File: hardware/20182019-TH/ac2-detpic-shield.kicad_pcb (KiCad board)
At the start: 2 copper layers, 99.1 x 69.6 mm, 57 parts, among them J1 HEADER, J2 HEADER, J3 HEADER, J4 HEADER, J5 HEADER, J6 HEADER, J7 HEADER, M1 M1, M2 M2, M3 MountingHole_2.2mm_M2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

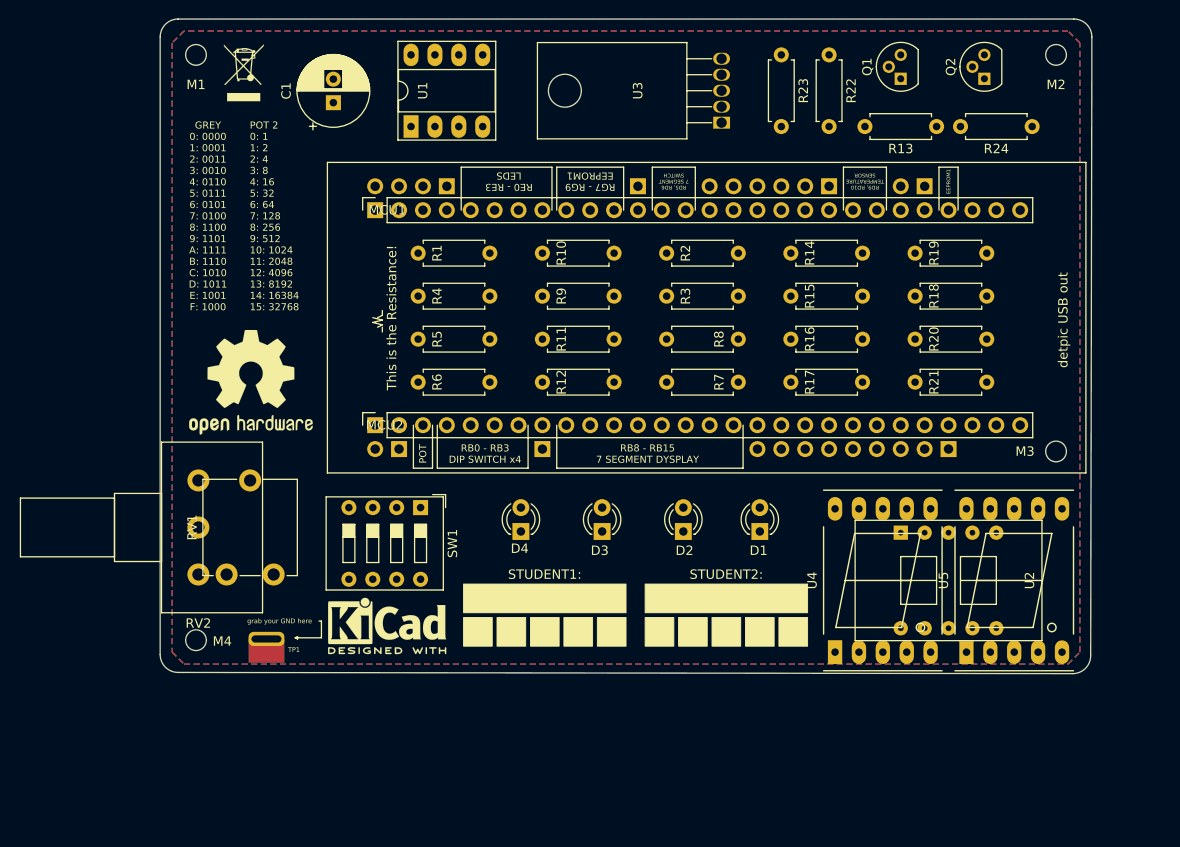
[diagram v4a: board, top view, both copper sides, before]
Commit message: small pcb organization of components
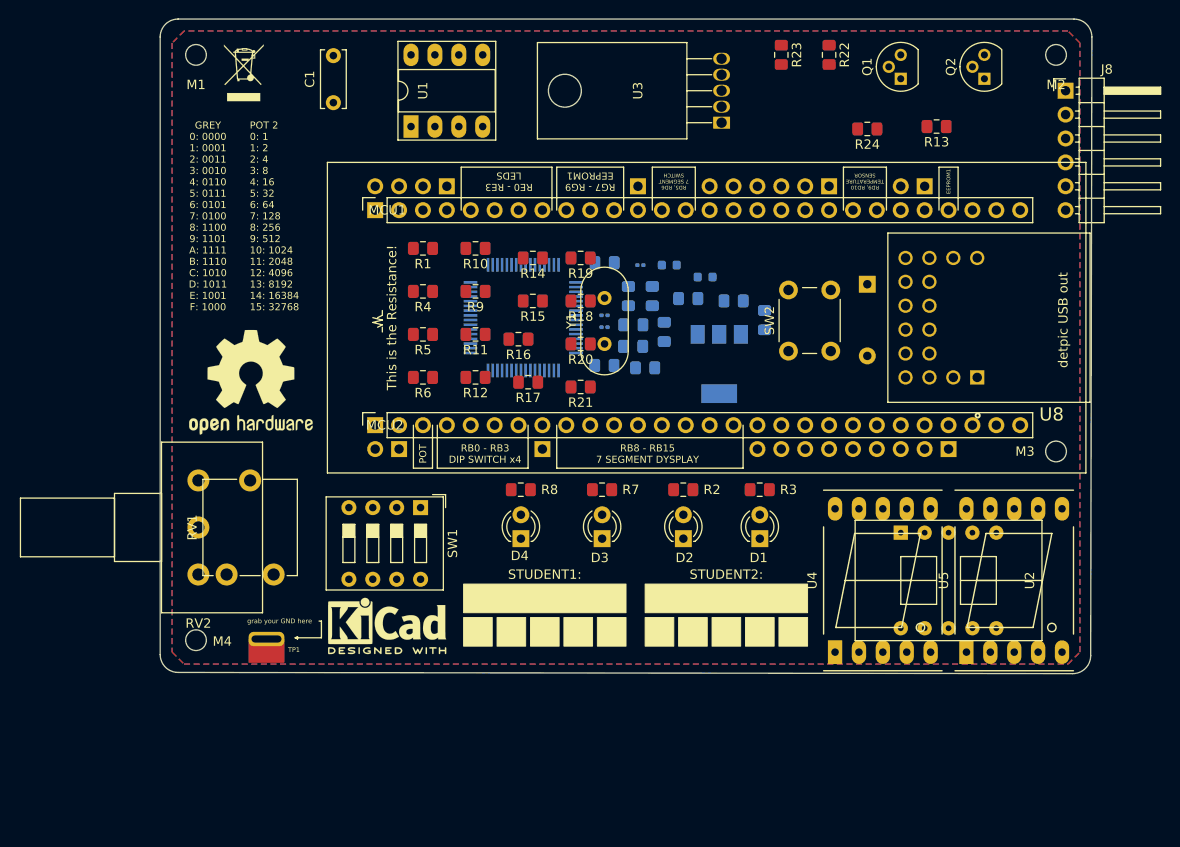
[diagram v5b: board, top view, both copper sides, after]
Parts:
- removed REF4: KiCad-Logo2_5mm_SilkScreen, Symbol:KiCad-Logo2_5mm_SilkScreen
- added C10: 20pF, Capacitor_SMD:C_0201_0603Metric, B.Cu at (174.2, 58.2)
- added C11: 20pF, Capacitor_SMD:C_0201_0603Metric, B.Cu at (178.1, 51.6)
- added C12: 0.1uF, Capacitor_SMD:C_0201_0603Metric, B.Cu at (174.2, 56.9)
- added C2: 0.1uF, Capacitor_SMD:C_0805_2012Metric_Pad1.15x1.40mm_HandSolder, B.Cu at (176.8, 54.9)
- added C3: 4.7uF, Capacitor_SMD:C_0805_2012Metric_Pad1.15x1.40mm_HandSolder, B.Cu at (174.3, 51.3)
- added C4: 0.1uF, Capacitor_SMD:C_0805_2012Metric_Pad1.15x1.40mm_HandSolder, B.Cu at (179.3, 54.9)
- added C5: 0.1uF, Capacitor_SMD:C_0805_2012Metric_Pad1.15x1.40mm_HandSolder, B.Cu at (174.2, 62.2)
- added C6: 4.7uF, Capacitor_SMD:C_0805_2012Metric_Pad1.15x1.40mm_HandSolder, B.Cu at (177.3, 60.2)
- added C7: 0.1uF, Capacitor_SMD:C_0805_2012Metric_Pad1.15x1.40mm_HandSolder, B.Cu at (191.3, 57.4)
- added C8: 0.1uF, Capacitor_SMD:C_0805_2012Metric_Pad1.15x1.40mm_HandSolder, B.Cu at (177.3, 57.9)
- added C9: 10uF, Capacitor_SMD:C_0805_2012Metric_Pad1.15x1.40mm_HandSolder, B.Cu at (180.6, 58.7)
- added D5: D_Small, Diode_THT:D_A-405_P7.62mm_Horizontal, B.Cu at (202.2, 53.6)
- added D6: LED, LED_SMD:LED_0603_1608Metric, B.Cu at (181.1, 51.6)
- added D7: LED, LED_SMD:LED_0603_1608Metric, B.Cu at (184.9, 52.8)
- added J8: MPLAB ICD3, Connector_PinHeader_2.54mm:PinHeader_1x06_P2.54mm_Horizontal, F.Cu at (223.3, 33.0)
- added R25: 4k7, Resistor_SMD:R_0805_2012Metric_Pad1.15x1.40mm_HandSolder, B.Cu at (178.6, 62.5)
- added R26: 330, Resistor_SMD:R_0805_2012Metric_Pad1.15x1.40mm_HandSolder, B.Cu at (183.1, 55.1)
- added R27: 330, Resistor_SMD:R_0805_2012Metric_Pad1.15x1.40mm_HandSolder, B.Cu at (188.0, 55.4)
- added SW2: SW_Push, Button_Switch_THT:SW_PUSH_6mm, F.Cu at (193.8, 60.7)
- added U6: PIC32MX795F512H-80V_PT, PIC32MX795F512H-80V_PT:TQFP64_10X10MC, B.Cu at (165.6, 57.1)
- added U7: TC1262-33, Package_TO_SOT_SMD:SOT-223, B.Cu at (186.4, 62.1)
- added U8: MM232R, MM232R:FTDI_MM232R, F.Cu at (215.1, 57.1)
- added Y1: 8MHz, Crystal:Crystal_HC49-4H_Vertical, F.Cu at (174.2, 59.9)
- C1: footprint Capacitor_THT:CP_Radial_D7.5mm_P2.50mm -> Capacitor_THT:C_Disc_D6.0mm_W2.5mm_P5.00mm
- R1, R10, R11, R12, R13, R14, R15, R16, R17, R18, R19, R2, R20, R21, R22, R23, R24, R3, R4, R5, R6, R7, R8, R9: footprint Resistor_THT:R_Axial_DIN0207_L6.3mm_D2.5mm_P7.62mm_Horizontal -> Resistor_SMD:R_0805_2012Metric_Pad1.15x1.40mm_HandSolder
- moved R18 43.2 mm to (171.7, 55.4)
- moved R19 43.2 mm to (171.7, 50.8)
- moved R20 43.2 mm to (171.7, 59.9)
- moved R21 43.2 mm to (171.7, 64.5)
- moved R16 36.6 mm to (165.1, 59.4)
- moved R17 35.6 mm to (166.1, 64.0)
- moved R14 35.1 mm to (166.6, 50.8)
- moved R15 35.1 mm to (166.6, 55.4)
- moved R2 25.8 mm to (182.6, 75.4)
- moved R8 22.3 mm to (165.3, 75.4)
- moved R3 20.7 mm to (190.7, 75.4)
- moved R24 17.5 mm to (202.2, 37.1)
- moved R10 14.7 mm to (160.5, 49.8)
- moved R11 14.7 mm to (160.5, 58.9)
- moved R12 14.7 mm to (160.5, 63.5)
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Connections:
- net /RB6 renamed /PGC
- net /RB7 renamed /PGD
- MCU1 pad 27: /+5V_EXT1 -> /+5V_EXT
- MCU2 pad 27: /+5V_EXT2 -> /+5V_EXT
- U5 pad 1: Net-(U5-Pad1) -> /7E
- U5 pad 10: Net-(U5-Pad10) -> /7G
- U5 pad 2: Net-(U5-Pad2) -> /7D
- U5 pad 4: Net-(U5-Pad4) -> /7C
- U5 pad 5: Net-(U5-Pad5) -> /7DP
- U5 pad 6: Net-(U5-Pad6) -> /7B
- U5 pad 7: Net-(U5-Pad7) -> /7A
- U5 pad 9: Net-(U5-Pad9) -> /7F

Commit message: some changes to pcb and footprints on pF caps to 0805
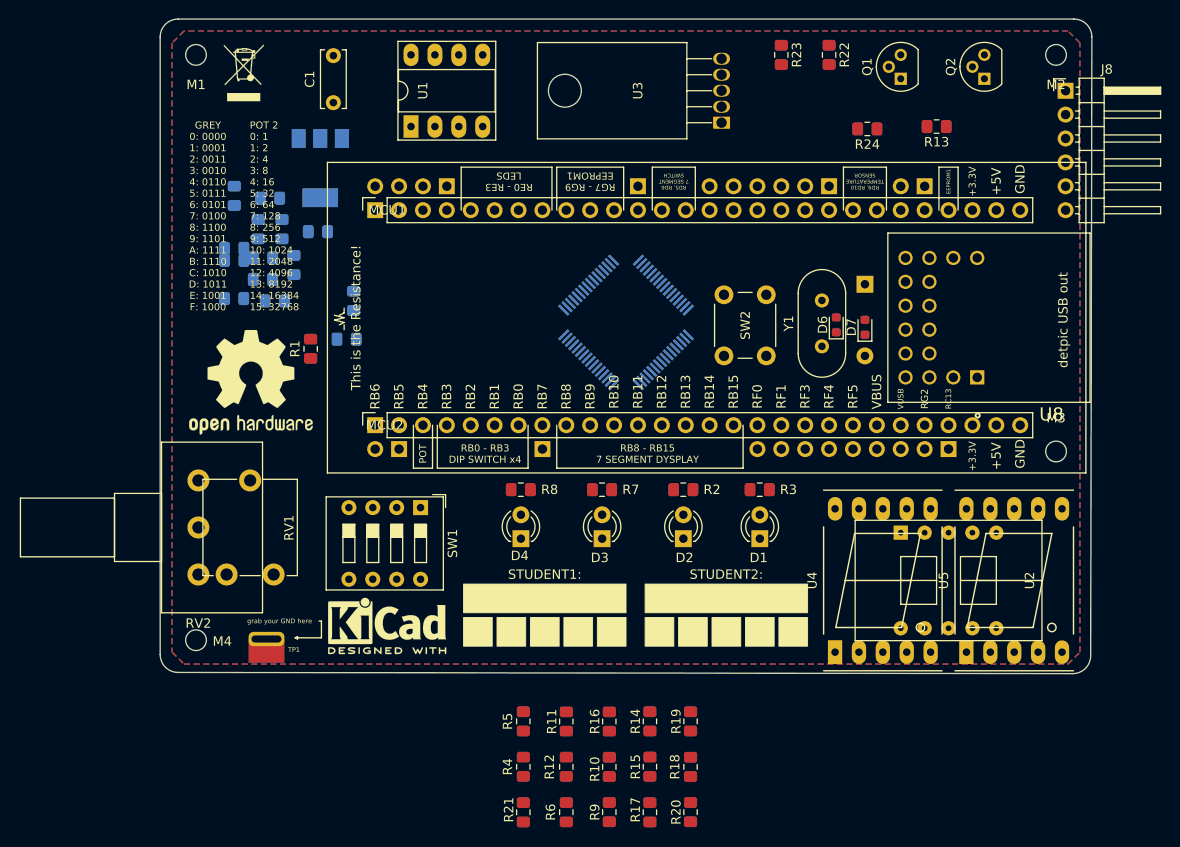
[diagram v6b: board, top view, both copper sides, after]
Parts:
- C10, C11, C12: footprint Capacitor_SMD:C_0201_0603Metric -> Capacitor_SMD:C_0805_2012Metric_Pad1.15x1.40mm_HandSolder
- D6, D7: moved to F.Cu
- moved R9 57.2 mm to (174.8, 109.7), turned to 270 degrees
- moved R10 56.9 mm to (174.8, 104.9), turned to 270 degrees
- moved R4 51.7 mm to (165.6, 104.9), turned to 90 degrees
- moved R20 51.1 mm to (183.4, 109.7), turned to 270 degrees
- moved R15 51.1 mm to (179.1, 104.9), turned to 270 degrees
- moved R18 50.9 mm to (183.4, 104.9), turned to 90 degrees
- moved R14 50.8 mm to (179.1, 100.1), turned to 270 degrees
- moved R19 50.6 mm to (183.4, 100.1), turned to 270 degrees
- moved R6 48.7 mm to (170.2, 109.7), turned to 90 degrees
- moved R17 47.5 mm to (179.1, 109.7), turned to 270 degrees
- moved U7 47.3 mm to (144.0, 41.2)
- moved R21 45.6 mm to (165.6, 109.7), turned to 270 degrees
- moved C7 43.7 mm to (147.6, 55.4)
- moved R12 42.5 mm to (170.2, 104.9), turned to 270 degrees
- moved R5 42.5 mm to (165.6, 100.1), turned to 90 degrees
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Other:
- board text added: "+3.3V"
- board text added: "+5V"
- board text added: "GND"
- board text added: "RB0"
- board text added: "RB1"
- board text added: "RB10"
- board text added: "RB11"
- board text added: "RB12"
- board text added: "RB13"
- board text added: "RB14"
- board text added: "RB15"
- board text added: "RB2"
- board text added: "RB3"
- board text added: "RB4"
- board text added: "RB5"
- board text added: "RB6"
- board text added: "RB7"
- board text added: "RB8"
- board text added: "RB9"
- board text added: "RC13"
- board text added: "RF0"
- board text added: "RF1"
- board text added: "RF3"
- board text added: "RF4"
- board text added: "RF5"
- board text added: "RG2"
- board text added: "VBUS"
- board text added: "VUSB"
